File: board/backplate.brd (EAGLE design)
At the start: 100 x 80 mm, 22 parts, among them IC1 MAX7219CNG, IC2 MAX7219CNG, IC3 MAX7219CNG, IC4 MAX7219CNG

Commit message: add greber
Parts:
- moved C8 78.1 mm to (10.3, 7.18), flipped to the bottom, turned to 270 degrees
- moved R3 70.5 mm to (3.67, 13.2)
- moved R1 62.9 mm to (4.60, 28.4), turned to 90 degrees
- moved R4 62.1 mm to (61.3, 14.7), turned to 180 degrees
- moved R2 45.6 mm to (58.0, 28.5), turned to 180 degrees
- moved J2 43.2 mm to (35.3, 23.7)
- moved C4 39.5 mm to (6.16, 36.4), flipped to the bottom, turned to 270 degrees
- moved J1 36.3 mm to (7.78, 23.9)
- moved JP2 33.2 mm to (64.9, 23.0)
- moved C5 30.9 mm to (59.2, 36.2), flipped to the bottom, turned to 270 degrees
- moved IC2 29.8 mm to (51.6, 36.2)
- moved IC4 28.9 mm to (51.9, 6.46)
- moved IC1 27.0 mm to (17.2, 36.2)
- moved IC3 25.2 mm to (17.2, 6.46)
- moved J4 25.2 mm to (39.4, 15.9)
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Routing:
- net GND: track 0.00 -> 221.3 mm
- net VCC: track 0.00 -> 211.2 mm, vias 0 -> 2
- net CS: track 0.00 -> 143.4 mm
- net CLK: track 0.00 -> 132.8 mm, vias 0 -> 1
- net N$71: track 0.00 -> 79.0 mm, vias 0 -> 2
- net N$21: track 0.00 -> 53.2 mm
- net N$72: track 0.00 -> 43.5 mm
- net N$70: track 0.00 -> 42.7 mm, vias 0 -> 1
- net N$5: track 0.00 -> 39.9 mm
- net N$51: track 0.00 -> 39.8 mm, vias 0 -> 2
- net N$7: track 0.00 -> 37.7 mm, vias 0 -> 1
- net DOUT: track 0.00 -> 37.2 mm
- net N$57: track 0.00 -> 35.5 mm
- net N$49: track 0.00 -> 33.4 mm
- net N$55: track 0.00 -> 32.3 mm
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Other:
- board size 100 x 80 mm -> 68.2 x 43.2 mm
- board text added: "DIN"
- board text added: "DOUT"
- board text added: "https://github.com/5shekel/monty"

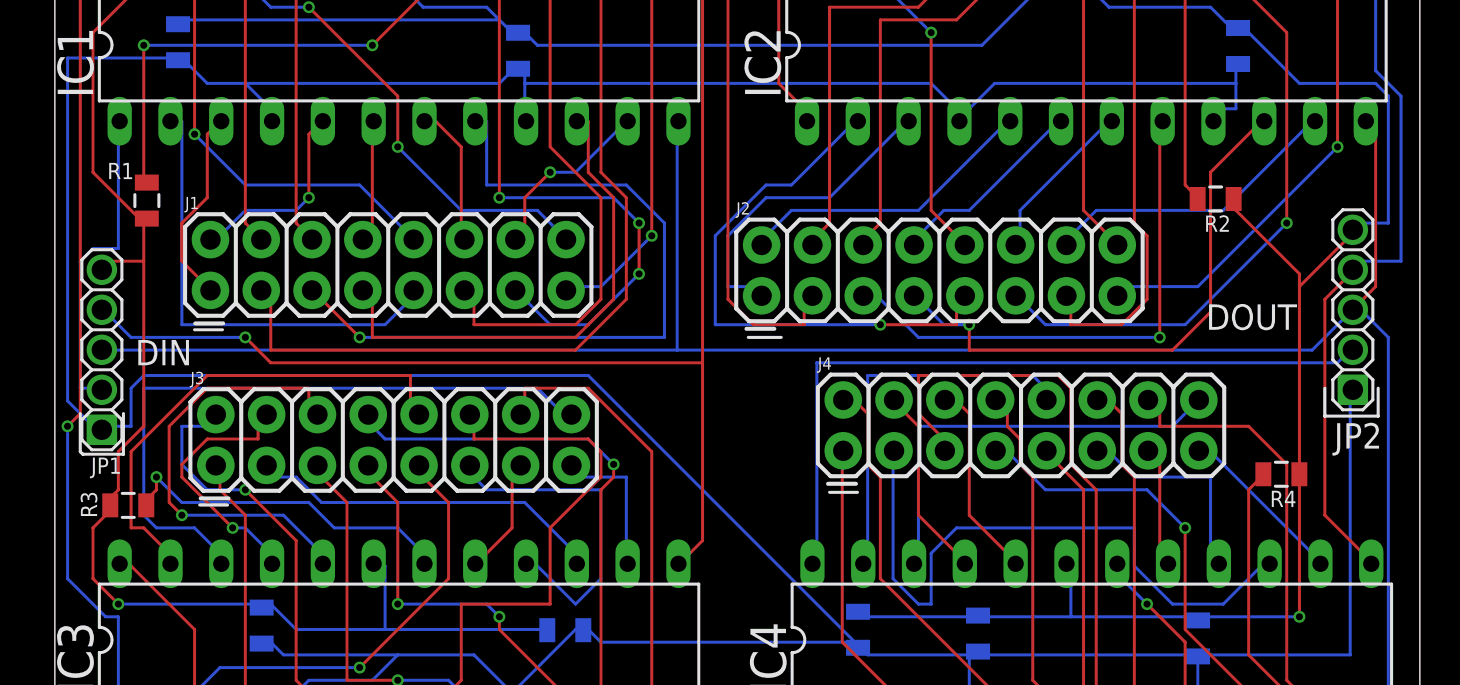
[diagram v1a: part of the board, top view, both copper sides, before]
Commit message: changed resistors to thru
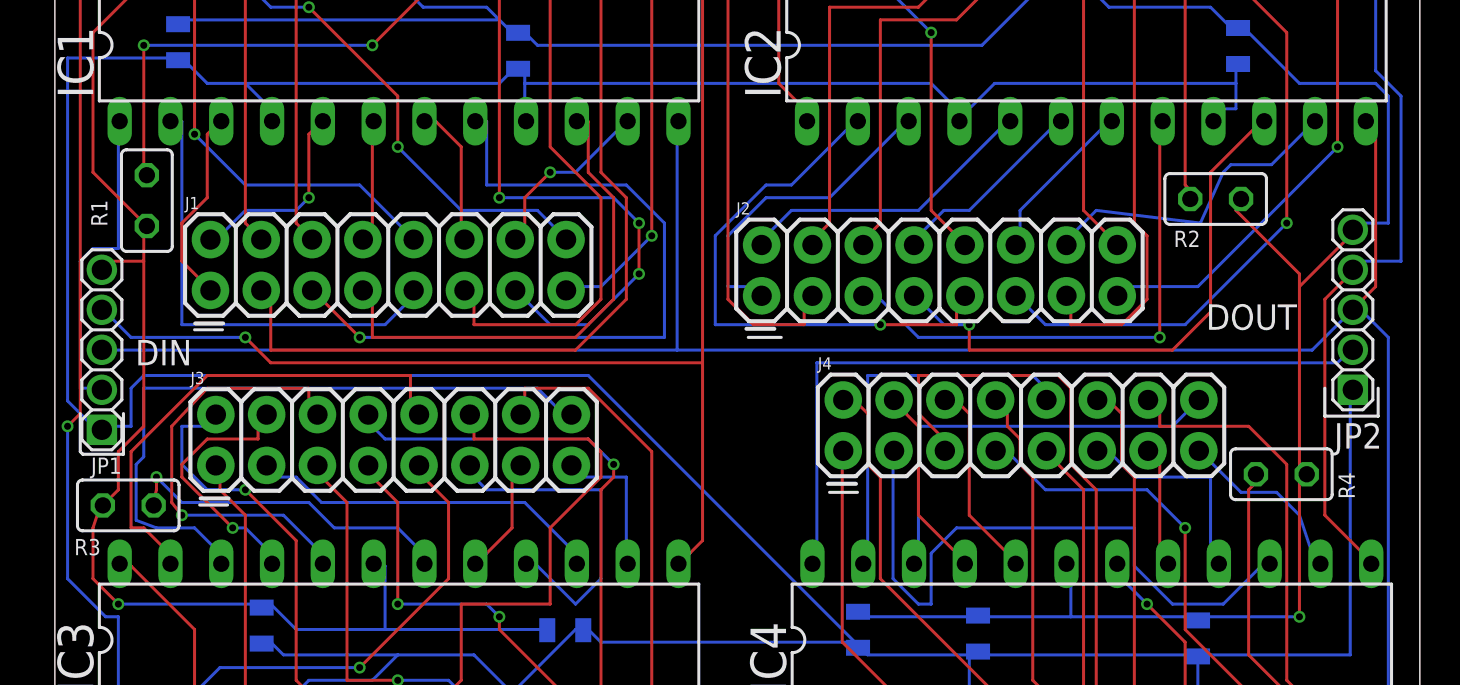
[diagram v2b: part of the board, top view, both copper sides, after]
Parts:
- R1, R2, R3, R4: device TinyTony_ShenzenReady:0805 -> rcl:V526-0
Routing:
- net N$31: track 15.1 -> 16.1 mm
- net N$67: track 8.44 -> 9.32 mm
- net N$49: track 33.4 -> 34.0 mm

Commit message: backplight v2
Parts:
- JP1, JP2: device pinhead:1_05X2MM -> SparkFun-Connectors:1X05
- moved C4 58.5 mm to (57.1, 7.62)
- moved R4 54.1 mm to (7.24, 15.4), turned to 90 degrees
- moved C8 40.6 mm to (39.4, 35.6)
- moved IC3 34.9 mm to (52.1, 6.35)
- moved C7 34.1 mm to (27.9, 35.6)
- moved J3 33.9 mm to (41.9, 16.5)
- moved C6 33.8 mm to (6.35, 7.62), turned to 0 degrees
- moved R3 33.3 mm to (36.8, 16.5), turned to 270 degrees
- moved IC4 32.8 mm to (19.1, 6.35)
- moved C3 32.2 mm to (43.2, 35.6)
- moved C5 28.7 mm to (62.2, 7.62)
- moved R1 26.8 mm to (31.3, 25.9)
- moved J4 26.7 mm to (12.7, 16.5)
- moved R2 21.4 mm to (36.8, 25.4), turned to 90 degrees
- moved JP2 7.81 mm to (66.0, 15.2)
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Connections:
- removed net N$13 (its old number): IC1.7, J1.12
- removed net N$17: IC1.14, J1.15
- removed net N$19 (its old number): IC2.3, J2.1
- removed net N$20 (its old number): IC2.5, J2.2
- removed net N$29: IC2.7, J2.12
- removed net N$31: IC2.11, J2.14
- removed net N$33 (its old number): IC2.14, J2.15
- removed net N$34: IC2.6, J2.8
- removed net N$40 (its old number): IC3.8, J3.5
- removed net N$41 (its old number): IC3.20, J3.6
- removed net N$58 (its old number): IC4.20, J4.6
- removed net N$59 (its old number): IC4.10, J4.7
- removed net N$63: IC4.7, J4.12
- removed net N$65: IC4.11, J4.14
- removed net N$68: IC4.6, J4.8
- new net N$2: IC1.23, J1.13
- new net N$28: IC2.5, J2.4
- new net N$35: IC2.23, J2.13
- new net N$45: IC3.6, J3.16
- new net N$62: IC4.11, J4.5
- new net N$69: IC4.10, J4.14
- new net N$71: IC1.20, J1.12
- new net N$72: IC4.5, J4.4
- new net N$73: IC4.8, J4.10
- new net N$74: IC4.14, J4.3
- new net N$76: IC4.23, J4.13
- new net N$77: IC4.21, J4.8
- new net N$78: IC4.15, J4.6
- new net N$79: IC4.17, J4.7
- new net N$80: IC4.22, J4.1
- net N$10: now also IC1.8; no longer IC1.23
- net N$11: now also IC1.14, J1.3; no longer IC1.2, J1.9
- net N$14: now also IC1.21, J1.8; no longer IC1.17, J1.13
- net N$15: now also IC1.15, J1.6; no longer IC1.11, J1.14
- net N$16: now also IC1.17, J1.7; no longer IC1.22, J1.16
- net N$18: now also IC1.22, J1.1; no longer IC1.6, J1.8
- net N$21: now also IC2.20, J2.12; no longer IC2.15, J2.3
- net N$22: now also IC2.2, J2.15; no longer IC2.21, J2.4
- net N$23: now also IC2.11; no longer IC2.8
- net N$24: now also IC2.6, J2.16; no longer IC2.20, J2.6
- net N$25: now also IC2.7, J2.9; no longer IC2.10, J2.7
- net N$26: now also IC2.3, J2.2; no longer IC2.23, J2.10
- net N$27: now also IC2.10, J2.14; no longer IC2.2, J2.9
- net N$3: now also IC1.2, J1.15; no longer IC1.3, J1.1
- net N$30: now also IC2.8, J2.10; no longer IC2.17, J2.13
- net N$32: now also IC2.14, J2.3; no longer IC2.22, J2.16
- net N$36: now also IC2.21, J2.8; no longer IC3.3, J3.1
- net N$37: now also IC2.15, J2.6; no longer IC3.5, J3.2
- net N$38: now also IC2.17, J2.7; no longer IC3.15, J3.3
- net N$39: now also IC2.22, J2.1; no longer IC3.21, J3.4
- net N$4: now also IC1.11, J1.5; no longer IC1.5, J1.2
- net N$42: now also IC3.20, J3.12; no longer IC3.10, J3.7
- net N$43: now also IC3.2, J3.15; no longer IC3.23, J3.10
- net N$44: now also IC3.11, J3.5; no longer IC3.2, J3.9
- net N$46: now also J3.9; no longer J3.12
- net N$47: now also IC3.3, J3.2; no longer IC3.17, J3.13
- net N$48: now also IC3.10; no longer IC3.11
- net N$49: now also IC3.5, J3.4; no longer IC3.22, J3.16
- net N$5: now also IC1.6, J1.16; no longer IC1.15, J1.3
- net N$50: now also IC3.8, J3.10; no longer IC3.14, J3.15
- net N$51: now also IC3.14, J3.3; no longer IC3.6, J3.8
- net N$53: now also IC3.23, J3.13; no longer IC4.3, J4.1
- net N$54: now also IC3.21, J3.8; no longer IC4.5, J4.2
- net N$55: now also IC3.15, J3.6; no longer IC4.15, J4.3
- net N$56: now also IC3.17, J3.7; no longer IC4.21, J4.4
- net N$57: now also IC3.22, J3.1; no longer IC4.8, J4.5
- net N$6: now also IC1.7, J1.9; no longer IC1.21, J1.4
- net N$60: now also IC4.20, J4.12; no longer IC4.23, J4.10
- net N$61: now also J4.15; no longer J4.9
- net N$64: now also IC4.6, J4.16; no longer IC4.17, J4.13
- net N$66: now also IC4.7, J4.9; no longer IC4.22, J4.16
- net N$67: now also IC4.3, J4.2; no longer IC4.14, J4.15
- net N$7: now also IC1.3, J1.2; no longer IC1.8, J1.5
- net N$8: now also IC1.10, J1.14; no longer IC1.20, J1.6
- net N$9: now also IC1.5, J1.4; no longer IC1.10, J1.7
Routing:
- net N$64: track 6.34 -> 50.3 mm
- net N$20: track 79.0 -> 38.7 mm, vias 2 -> 0
- net DOUT: track 37.2 -> 74.4 mm
- net N$2: track 0.00 -> 35.2 mm, vias 0 -> 1
- net N$35: track 0.00 -> 35.2 mm
- net N$3: track 9.89 -> 42.7 mm
- net N$7: track 37.7 -> 5.08 mm, vias 1 -> 0
- net N$45: track 0.00 -> 29.3 mm
- net N$76: track 0.00 -> 28.9 mm
- net N$16: track 24.3 -> 53.2 mm, vias 2 -> 0
- net N$21: track 53.2 -> 24.4 mm
- net N$57: track 35.5 -> 6.88 mm
- net N$62: track 0.00 -> 27.8 mm, vias 0 -> 1
- net N$79: track 0.00 -> 27.5 mm
- net N$74: track 0.00 -> 27.4 mm
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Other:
- board text added: "Din"
- board text removed: "DIN"

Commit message: based on https://i.imgur.com/TE96g29.png" "
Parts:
- removed C3, C5, C7: 10uF, TinyTony_ShenzenReady:0805
- removed C4, C6, C8: .1uF, TinyTony_ShenzenReady:0805
- removed IC2, IC3, IC4: MAX7219CNG, maxim:DIL24-3
- removed J2, J3, J4: (no value), SparkFun-Connectors:2X8
- removed R2, R3, R4: 33k, rcl:V526-0
- J1: device SparkFun-Connectors:2X8 -> backplate:2X8
- moved J1 1.27 mm to (9.05, 23.9)
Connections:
- removed net N$18: IC1.22, J1.1
- removed net N$19: IC2.18, R2.2
- removed net N$20: IC2.24, IC3.1
- removed net N$21: IC2.20, J2.12
- removed net N$22: IC2.2, J2.15
- removed net N$23: IC2.11, J2.5
- removed net N$24: IC2.6, J2.16
- removed net N$25: IC2.7, J2.9
- removed net N$26: IC2.3, J2.2
- removed net N$27: IC2.10, J2.14
- removed net N$28: IC2.5, J2.4
- removed net N$30: IC2.8, J2.10
- removed net N$32: IC2.14, J2.3
- removed net N$33: IC2.16, J2.11
- removed net N$35: IC2.23, J2.13
- removed net N$36: IC2.21, J2.8
- removed net N$37: IC2.15, J2.6
- removed net N$38: IC2.17, J2.7
- removed net N$39: IC2.22, J2.1
- removed net N$40: IC3.18, R3.2
- removed net N$41: IC1.24, IC2.1
- removed net N$42: IC3.20, J3.12
- removed net N$43: IC3.2, J3.15
- removed net N$44: IC3.11, J3.5
- removed net N$45: IC3.6, J3.16
- removed net N$46: IC3.7, J3.9
- removed net N$47: IC3.3, J3.2
- removed net N$48: IC3.10, J3.14
- removed net N$49: IC3.5, J3.4
- removed net N$50: IC3.8, J3.10
- removed net N$51: IC3.14, J3.3
- removed net N$52: IC3.16, J3.11
- removed net N$53: IC3.23, J3.13
- removed net N$54: IC3.21, J3.8
- removed net N$55: IC3.15, J3.6
- removed net N$56: IC3.17, J3.7
- removed net N$57: IC3.22, J3.1
- removed net N$58: IC4.18, R4.2
- removed net N$59: IC3.24, IC4.1
- removed net N$60: IC4.20, J4.12
- removed net N$61: IC4.2, J4.15
- removed net N$62: IC4.11, J4.5
- removed net N$64: IC4.6, J4.16
- removed net N$66: IC4.7, J4.9
- removed net N$67: IC4.3, J4.2
- removed net N$69: IC4.10, J4.14
- removed net N$72: IC4.5, J4.4
- removed net N$73: IC4.8, J4.10
- removed net N$74: IC4.14, J4.3
- removed net N$75: IC4.16, J4.11
- removed net N$76: IC4.23, J4.13
- removed net N$77: IC4.21, J4.8
- removed net N$78: IC4.15, J4.6
- removed net N$79: IC4.17, J4.7
- removed net N$80: IC4.22, J4.1
- new net N$17: IC1.22, J1.9
- net CLK: no longer IC2.13, IC3.13, IC4.13
- net CS: no longer IC2.12, IC3.12, IC4.12
- net DOUT: now also IC1.24; no longer IC4.24
- net GND: no longer C3.2, C4.2, C5.2, C6.2, C7.2, C8.2, IC2.4, IC2.9, IC3.4, IC3.9, IC4.4, IC4.9
- net N$10: now also IC1.14, J1.14; no longer IC1.8, J1.10
- net N$11: now also IC1.16, J1.8; no longer IC1.14, J1.3
- net N$13: now also IC1.23, J1.1; no longer IC1.16, J1.11
- net N$14: now also J1.7; no longer J1.8
- net N$15: now also J1.2; no longer J1.6
- net N$16: now also J1.5; no longer J1.7
- net N$2: now also IC1.2; no longer IC1.23
- net N$3: now also IC1.11, J1.3; no longer IC1.2, J1.15
- net N$4: now also IC1.6, J1.4; no longer IC1.11, J1.5
- net N$5: now also IC1.7, J1.10; no longer IC1.6, J1.16
- net N$6: now also IC1.3, J1.6; no longer IC1.7, J1.9
- net N$7: now also IC1.10, J1.11; no longer IC1.3, J1.2
- net N$8: now also IC1.5, J1.15; no longer IC1.10, J1.14
- net N$9: now also IC1.8, J1.16; no longer IC1.5, J1.4
- net VCC: no longer C3.1, C4.1, C5.1, C6.1, C7.1, C8.1, IC2.19, IC3.19, IC4.19, R2.1, R3.1, R4.1
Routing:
- net VCC: track 236.4 -> 0.00 mm
- net GND: track 194.2 -> 0.00 mm
- net CLK: track 150.7 -> 0.00 mm
- net CS: track 134.0 -> 0.00 mm
- net DOUT: track 74.4 -> 0.00 mm
- net N$16: track 53.2 -> 0.00 mm
- net N$64: track 50.3 -> 0.00 mm
- net N$41: track 47.6 -> 0.00 mm
- net N$3: track 42.7 -> 0.00 mm
- net N$20: track 38.7 -> 0.00 mm
- net N$11: track 37.7 -> 0.00 mm
- net N$59: track 37.5 -> 0.00 mm, vias 1 -> 0
- net N$15: track 35.5 -> 0.00 mm
- net N$2: track 35.2 -> 0.00 mm, vias 1 -> 0
- net N$35: track 35.2 -> 0.00 mm
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
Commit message: routed 4
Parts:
- added C3, C5, C7: 10uF, TinyTony_ShenzenReady:0805
- added C4, C6, C8: .1uF, TinyTony_ShenzenReady:0805
- added IC2, IC3, IC4: MAX7219CNG, maxim:DIL24-3
- added J2, J3, J4: (no value), backplate:2X8
- added R2, R3, R4: 33k, rcl:V526-0
- moved C2 29.3 mm to (28.0, 36.1)
- moved J1 1.44 mm to (7.62, 24.1)
- moved C1 1.15 mm to (24.3, 36.0)
- moved IC1 0.94 mm to (16.5, 36.8)
- moved R1 0.69 mm to (31.8, 25.4)
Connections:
- new net FF: IC1.24, IC2.1
- new net N$18: IC2.18, R2.2
- new net N$19: IC2.2, J2.13
- new net N$20: IC2.11, J2.3
- new net N$21: IC2.6, J2.4
- new net N$22: IC2.7, J2.10
- new net N$23: IC2.3, J2.6
- new net N$24: IC2.10, J2.11
- new net N$25: IC2.5, J2.15
- new net N$26: IC2.8, J2.16
- new net N$27: IC2.14, J2.14
- new net N$28: IC2.16, J2.8
- new net N$29: IC2.20, J2.12
- new net N$30: IC2.23, J2.1
- new net N$31: IC2.21, J2.7
- new net N$32: IC2.15, J2.2
- new net N$33: IC2.17, J2.5
- new net N$34: IC2.22, J2.9
- new net N$35: IC3.18, R3.2
- new net N$36: IC3.2, J3.13
- new net N$37: IC3.11, J3.3
- new net N$38: IC3.6, J3.4
- new net N$39: IC3.7, J3.10
- new net N$40: IC3.3, J3.6
- new net N$41: IC3.10, J3.11
- new net N$42: IC3.5, J3.15
- new net N$43: IC3.8, J3.16
- new net N$44: IC3.14, J3.14
- new net N$45: IC3.16, J3.8
- new net N$46: IC3.20, J3.12
- new net N$47: IC3.23, J3.1
- new net N$48: IC3.21, J3.7
- new net N$49: IC3.15, J3.2
- new net N$50: IC3.17, J3.5
- new net N$51: IC3.22, J3.9
- new net N$52: IC4.18, R4.2
- new net N$53: IC4.2, J4.13
- new net N$54: IC4.11, J4.3
- new net N$55: IC4.6, J4.4
- new net N$56: IC4.7, J4.10
- new net N$57: IC4.3, J4.6
- new net N$58: IC4.10, J4.11
- new net N$59: IC4.5, J4.15
- new net N$60: IC4.8, J4.16
- new net N$61: IC4.14, J4.14
- new net N$62: IC4.16, J4.8
- new net N$63: IC4.20, J4.12
- new net N$64: IC4.23, J4.1
- new net N$65: IC4.21, J4.7
- new net N$66: IC4.15, J4.2
- new net N$67: IC4.17, J4.5
- new net N$68: IC4.22, J4.9
- new net N$69: IC2.24, IC4.1
- new net N$70: IC3.1, IC4.24
- net CLK: now also IC2.13, IC3.13, IC4.13
- net CS: now also IC2.12, IC3.12, IC4.12
- net DOUT: now also IC3.24; no longer IC1.24
- net GND: now also C3.2, C4.2, C5.2, C6.2, C7.2, C8.2, IC2.4, IC2.9, IC3.4, IC3.9, IC4.4, IC4.9
- net VCC: now also C3.1, C4.1, C5.1, C6.1, C7.1, C8.1, IC2.19, IC3.19, IC4.19, R2.1, R3.1, R4.1
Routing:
- net VCC: track 0.00 -> 207.1 mm, vias 0 -> 1
- net GND: track 0.00 -> 200.8 mm, vias 0 -> 2
- net CLK: track 0.00 -> 143.0 mm
- net CS: track 0.00 -> 127.8 mm, vias 0 -> 1
- net DOUT: track 0.00 -> 71.9 mm, vias 0 -> 2
- net FF: track 0.00 -> 58.8 mm, vias 0 -> 2
- net N$70: track 0.00 -> 54.4 mm, vias 0 -> 1
- net N$54: track 0.00 -> 45.1 mm
- net N$69: track 0.00 -> 40.2 mm
- net N$15: track 0.00 -> 39.1 mm, vias 0 -> 1
- net N$59: track 0.00 -> 38.0 mm, vias 0 -> 1
- net N$53: track 0.00 -> 37.8 mm, vias 0 -> 1
- net N$37: track 0.00 -> 37.4 mm, vias 0 -> 1
- net N$35: track 0.00 -> 36.5 mm
- net N$36: track 0.00 -> 36.2 mm
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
